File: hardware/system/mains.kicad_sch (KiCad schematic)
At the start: 10 parts, among them M1 Mains inlet, M2 RCD, M3 E-stop mushroom NC, M4 PSU 24-36 V, M5 Bit-change key switch, M6 Router contactor, M7 RC snubber, M8 Router socket, M9 PE: enclosure + lift frame

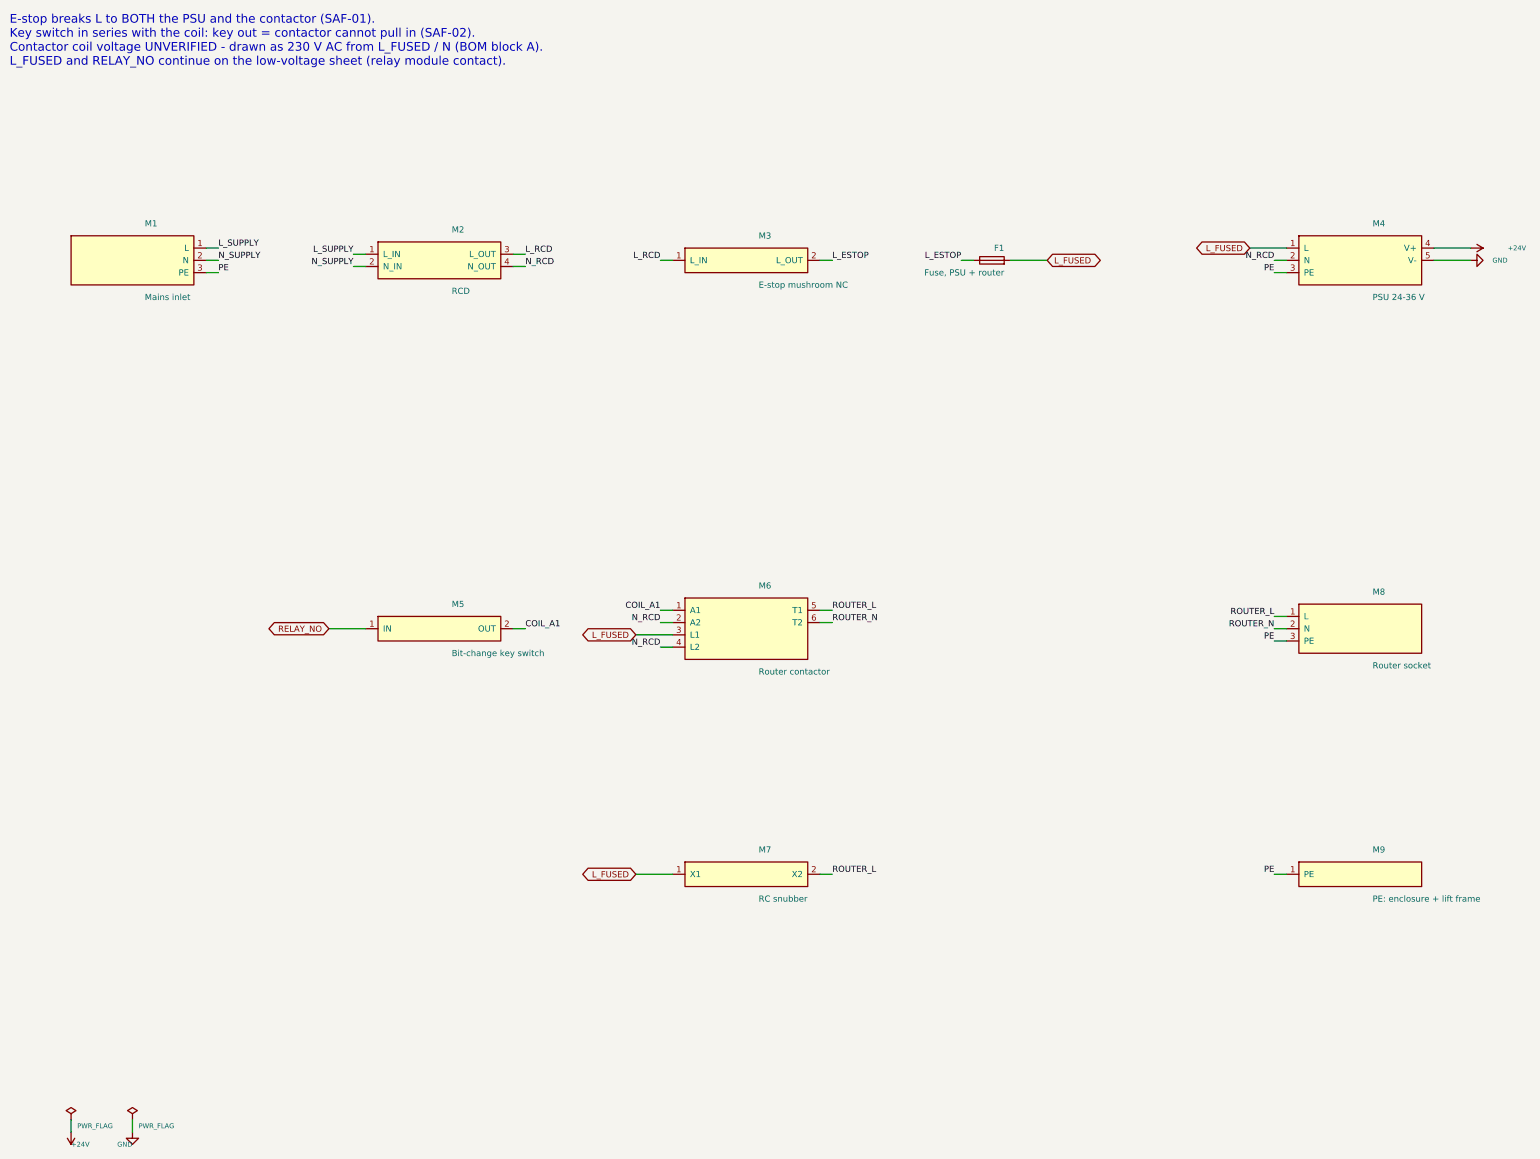
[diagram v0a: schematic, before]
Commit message: fix(hardware): regenerate schematics, symbol library and PDFs
Regenerated output of the preceding fix-wave commits (contactor topology,
devkit pin order, field_gap/arrow-legibility fixes, 74LVC14 fields,
zero-length wire removal). ERC clean (0 violations on all three projects)
and check_pins reports 0 mismatches.

Co-Authored-By: Claude Opus 5 (1M context) <noreply@anthropic.com>
Claude-Session: https://claude.ai/code/session_01N1nWXzYgvFT6pqfHGhLK6P
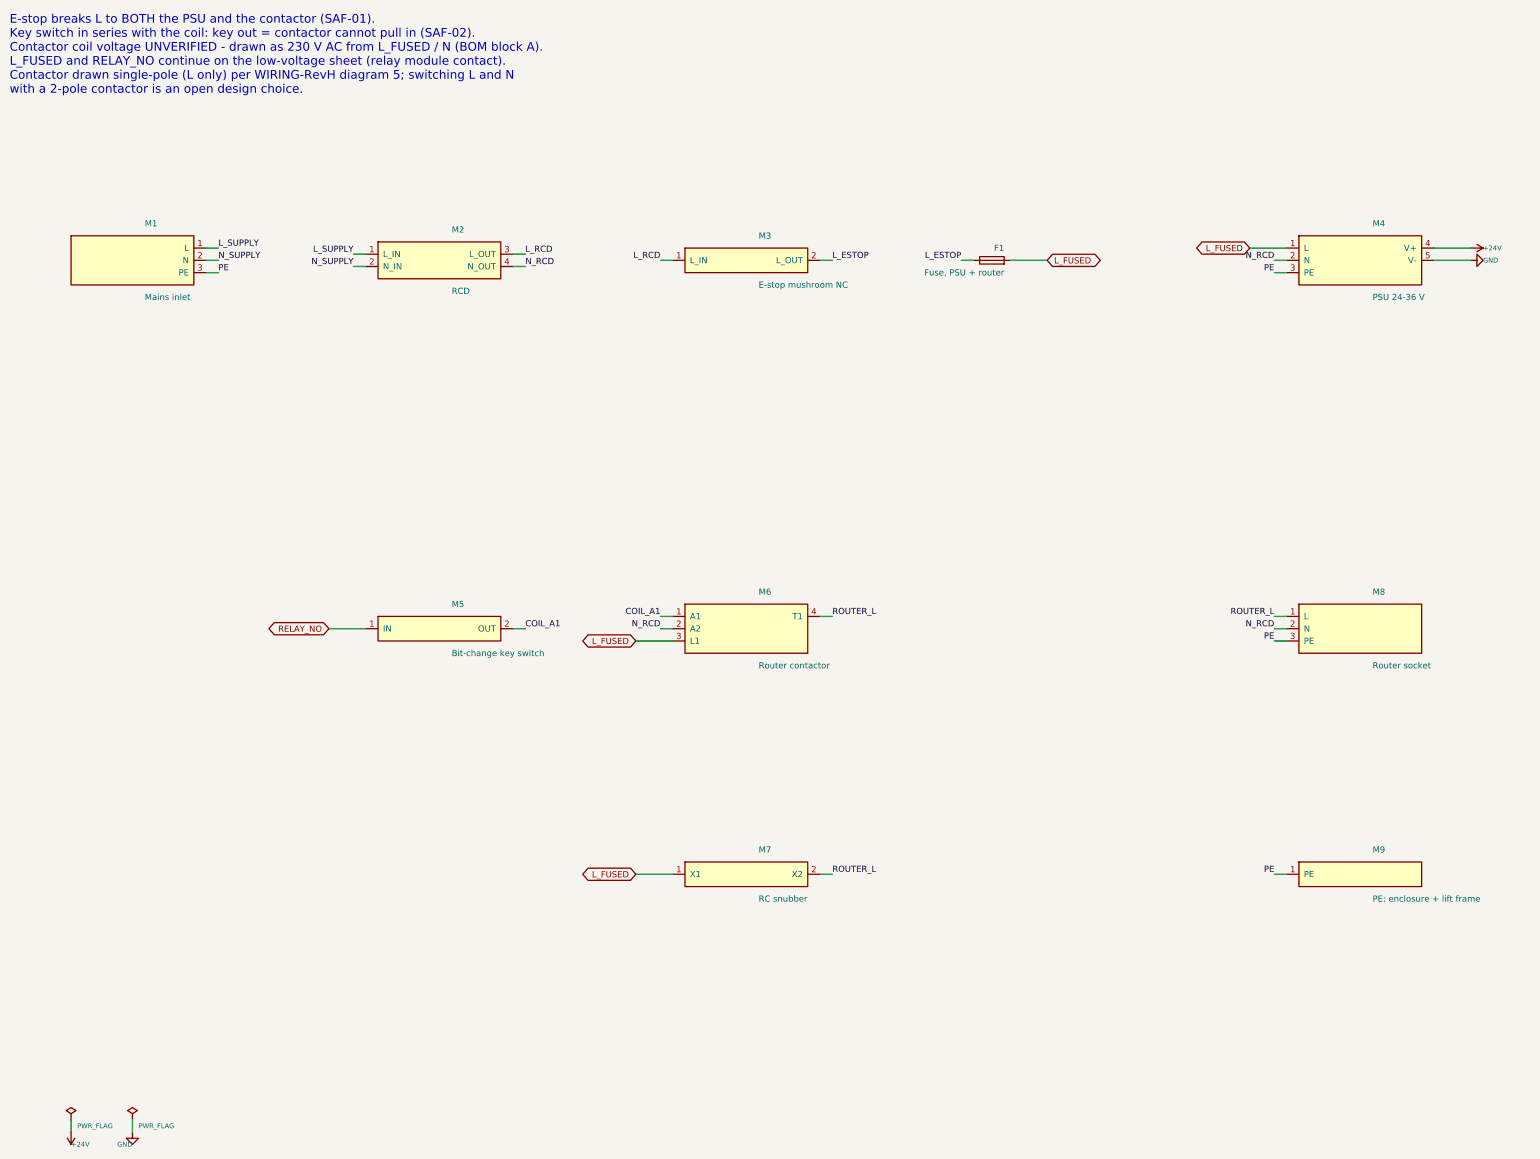
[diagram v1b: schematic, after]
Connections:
- net N_RCD: now also M8.2 (N); no longer M6.4 (L2)
- net ROUTER_L: now also M6.4 (T1); no longer M6.5 (T1)
- removed net ROUTER_N: M6.6 (T2), M8.2 (N)
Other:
- note added: "E-stop breaks L to BOTH the PSU and the contactor (SAF-01). Key switch in series with the coil: key out = contactor cannot pull in (SAF-02). Contactor coil voltage UNVERIFIED - drawn as 230 V AC from L_FUSED / N (BOM block A). L_FUSED and RELAY_NO continue on the low-voltage sheet (relay module contact). Contactor drawn single-pole (L only) per WIRING-RevH diagram 5; switching L and N with a 2-po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"
- note removed: "E-stop breaks L to BOTH the PSU and the contactor (SAF-01). Key switch in series with the coil: key out = contactor cannot pull in (SAF-02). Contactor coil voltage UNVERIFIED - drawn as 230 V AC from L_FUSED / N (BOM block A). L_FUSED and RELAY_NO continue on the low-voltage sheet (relay module contact)."
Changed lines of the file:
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@@
 	(wire
 		(pts
-			(xy 162.56 148.59)
-			(xy 160.02 148.59))
+			(xy 162.56 149.86)
+			(xy 160.02 149.86))
 		(stroke
 			(width 0)
@@
 )
 	(label "COIL_A1"
-		(at 160.02 148.59 180)
+		(at 160.02 149.86 180)
 		(effects
 			(font
@@
 	(wire
 		(pts
-			(xy 162.56 151.13)
-			(xy 160.02 151.13))
+			(xy 162.56 152.4)
+			(xy 160.02 152.4))
 		(stroke
 			(width 0)
@@
 )
 	(label "N_RCD"
-		(at 160.02 151.13 180)
+		(at 160.02 152.4 180)
 		(effects
 			(font
@@
 	(wire
 		(pts
-			(xy 162.56 153.67)
-			(xy 154.94 153.67))
+			(xy 162.56 154.94)
+			(xy 154.94 154.94))
 		(stroke
 			(width 0)
@@
 	(global_label "L_FUSED"
 		(shape bidirectional)
-		(at 154.94 153.67 180)
+		(at 154.94 154.94 180)
 		(effects
 			(font
@@
 			(justify right))
 		(property "Intersheetrefs" "${INTERSHEET_REFS}"
-			(at 154.94 153.67 0)
+			(at 154.94 154.94 0)
 			(effects
 				(font
@@
 	(wire
 		(pts
-			(xy 162.56 156.21)
-			(xy 160.02 156.21))
-		(stroke
-			(width 0)
-			(type default))
-)
-	(label "N_RCD"
-		(at 160.02 156.21 180)
-		(effects
-			(font
-				(size 1.27 1.27))
-			(justify right bottom))
-)
-	(wire
-		(pts
-			(xy 193.04 148.59)
-			(xy 195.58 148.59))
+			(xy 193.04 149.86)
+			(xy 195.58 149.86))
 		(stroke
 			(width 0)
@@
 )
 	(label "ROUTER_L"
-		(at 195.58 148.59 0)
-		(effects
-			(font
-				(size 1.27 1.27))
-			(justify left bottom))
-)
-	(wire
-		(pts
-			(xy 193.04 151.13)
-			(xy 195.58 151.13))
-		(stroke
-			(width 0)
-			(type default))
-)
-	(label "ROUTER_N"
-		(at 195.58 151.13 0)
+		(at 195.58 149.86 0)
 		(effects
 			(font
@@
 			(type default))
 )
-	(label "ROUTER_N"
+	(label "N_RCD"
 		(at 287.02 152.4 180)
 		(effects
@@
 			(type default))
 )
-	(text "E-stop breaks L to BOTH the PSU and the contactor (SAF-01).\nKey switch in series with the coil: key out = contactor cannot pull in (SAF-02).\nContactor coil voltage UNVERIFIED - drawn as 230 V AC from L_FUSED / N (BOM block A).\nL_FUSED and RELAY_NO continue on the low-voltage sheet (relay module contact)."
+	(text "E-stop breaks L to BOTH the PSU and the contactor (SAF-01).\nKey switch in series with the coil: key out = contactor cannot pull in (SAF-02).\nContactor coil voltage UNVERIFIED - drawn as 230 V AC from L_FUSED / N (BOM block A).\nL_FUSED and RELAY_NO continue on the low-voltage sheet (relay module contact).\nContactor drawn single-pole (L only) per WIRING-RevH diagram 5; switching L and N\nwith a 2-pole contactor is an open design choice."
 		(exclude_from_sim no)
 		(at 25.4 25.4 0)
@@
 				(hide yes)))
 		(property "Value" "+24V"
-			(at 335.28 73.66 90)
+			(at 330.2 73.66 90)
 			(effects
 				(font
@@
 				(hide yes)))
 		(property "Value" "GND"
-			(at 335.28 76.2 90)
+			(at 330.2 76.2 90)
 			(effects
 				(font
 					(size 1 1))
-				(justify left)))
+				(justify right)))
 		(property "Footprint" ""
 			(at 327.66 76.2 90)
@@
 		(dnp no)
 		(property "Reference" "M6"
-			(at 180.34 143.51 0)
+			(at 180.34 144.78 0)
 			(effects
 				(font
@@
 				(justify left)))
 		(property "Value" "Router contactor"
-			(at 180.34 161.29 0)
+			(at 180.34 160.02 0)
 			(effects
 				(font
@@
 		(pin "4"
 )
-		(pin "5"
-)
-		(pin "6"
-)
-		(instances
+		(instances
